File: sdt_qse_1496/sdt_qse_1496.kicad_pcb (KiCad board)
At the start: 2 copper layers, 100 x 70 mm, 88 parts, among them J1 Conn_02x08_Odd_Even, J2 SJ-3524-SMT, J3 5-1814832-1, J4 5-1814832-1, J6 Conn_01x02_Male, Q1 Q_NPN_BEC, Q2 Q_NPN_BEC, Q3 Q_PMOS_GSD, Q4 Q_PMOS_GSD, U1 SN74AC74PW, U2 MC1496DR2G, U3 Toroidal_Transformer, U4 MC1496DR2G

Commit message: Released to fab.
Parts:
- added C13: 0.1uF, Capacitor_SMD:C_1206_3216Metric, F.Cu at (120.5, 85.2)
- added C14: 0.1uF, Capacitor_SMD:C_1206_3216Metric, F.Cu at (116.1, 77.1)
- added R13: 100, Resistor_SMD:R_1206_3216Metric, F.Cu at (160.3, 117.3)
- added R15: 100, Resistor_SMD:R_1206_3216Metric, F.Cu at (146.1, 120.4)
- added R18: 100, Resistor_SMD:R_1206_3216Metric, F.Cu at (172.2, 122.8)
- moved R9 6.47 mm to (140.9, 87.8)
- moved R10 3.48 mm to (172.2, 126.3)
- moved C19 1.41 mm to (158.5, 111.8)
- moved C15 1.30 mm to (163.3, 113.4)
- moved R24 0.53 mm to (154.2, 108.9)
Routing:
- net Net-(R14-Pad1): track 23.9 -> 17.6 mm
- net GND: track 0.00 -> 4.88 mm, vias 65 -> 73
- net Net-(R10-Pad2): track 14.9 -> 19.1 mm
- net Net-(C4-Pad2): track 10.9 -> 14.4 mm
- net Net-(R8-Pad2): track 5.77 -> 9.08 mm
- net Net-(C8-Pad2): track 8.51 -> 11.1 mm
- net Net-(R12-Pad2): track 14.8 -> 17.1 mm
- net Net-(R62-Pad2): track 8.84 -> 10.7 mm
- net Net-(C15-Pad1): track 36.1 -> 34.5 mm
- net /12Vswitched: track 97.5 -> 96.6 mm
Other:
- board text added: "GREG KF5N"
- board text added: "PROTOTYPE 1"
- board text added: "QSE MC1496 EXCITER"

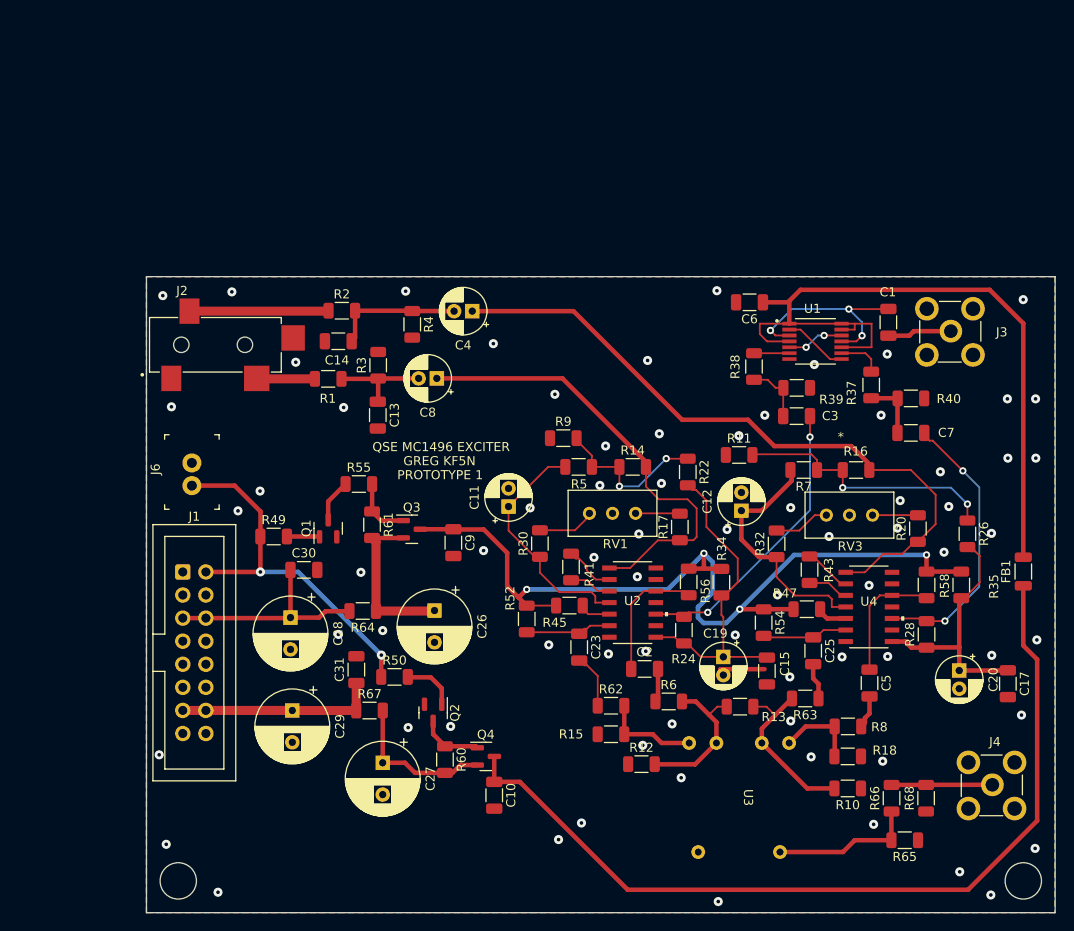
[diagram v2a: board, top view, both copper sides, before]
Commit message: Finishing layout of version2.
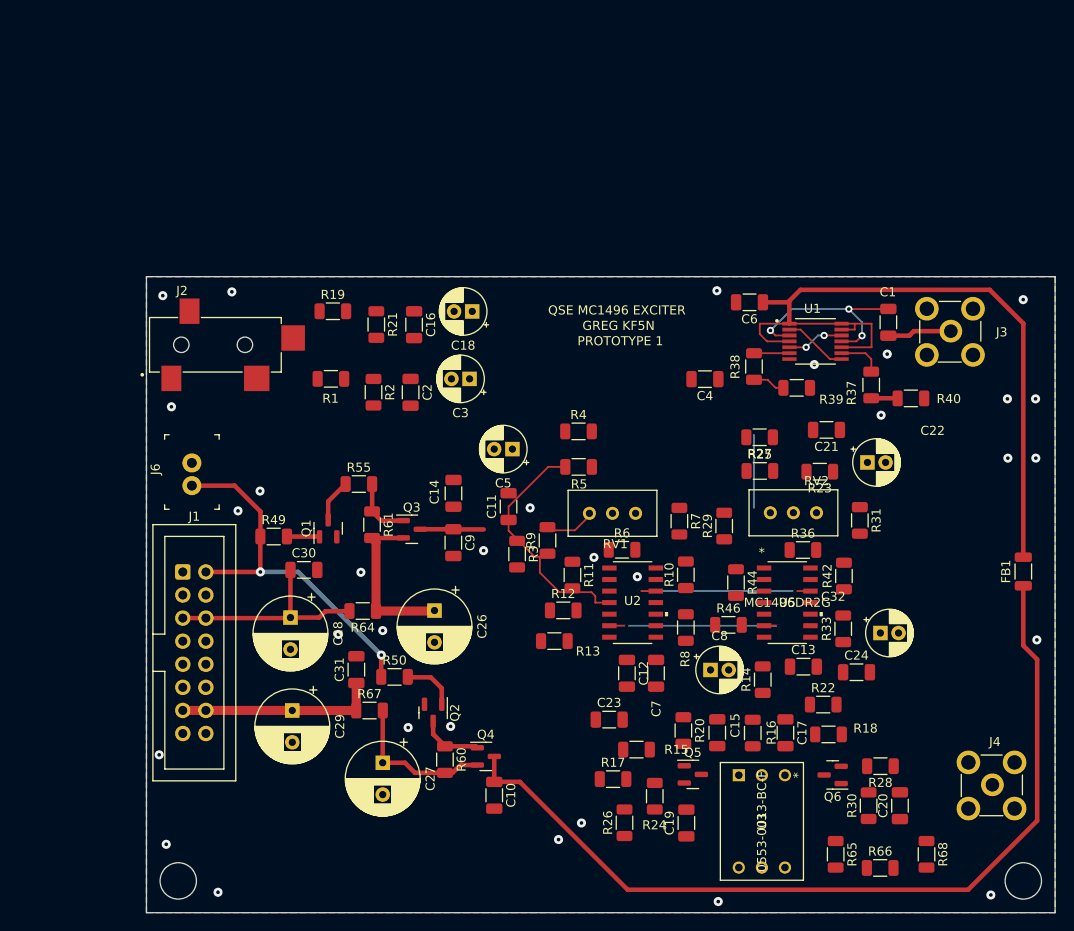
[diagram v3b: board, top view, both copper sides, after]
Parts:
- removed C25: 0.1uF, Capacitor_SMD:C_1206_3216Metric
- removed R32, R45, R47: 10k, Resistor_SMD:R_1206_3216Metric
- removed R34, R35: 1.3k, Resistor_SMD:R_1206_3216Metric
- removed R41, R43: 1.0k, Resistor_SMD:R_1206_3216Metric
- removed R52, R54, R56, R58: 3k, Resistor_SMD:R_1206_3216Metric
- removed R62, R63: 100, Resistor_SMD:R_1206_3216Metric
- removed RV3: 50k, Potentiometer_THT:Potentiometer_Bourns_3296W_Vertical
- removed U4: MC1496DR2G, MC1496:MC1496DR2G
- added C16: DNP, Capacitor_SMD:C_1206_3216Metric, F.Cu at (124.5, 75.3)
- added C18: 25uF 25V, Capacitor_THT:CP_Radial_D5.0mm_P2.00mm, F.Cu at (130.9, 73.8)
- added C21: 0.1uF, Capacitor_SMD:C_1206_3216Metric, F.Cu at (169.8, 86.9)
- added C22: 25uF 25V, Capacitor_THT:CP_Radial_D5.0mm_P2.00mm, F.Cu at (174.3, 90.5)
- added C24: 0.1uF, Capacitor_SMD:C_1206_3216Metric, F.Cu at (173.1, 113.5)
- added C32: 25uF 25V, Capacitor_THT:CP_Radial_D5.0mm_P2.00mm, F.Cu at (175.8, 109.2)
- added Q5: Q_NPN_BEC, Package_TO_SOT_SMD:SOT-23, F.Cu at (155.1, 124.8)
- added Q6: Q_NPN_BEC, Package_TO_SOT_SMD:SOT-23, F.Cu at (170.5, 124.8)
- added R19: 0, Resistor_SMD:R_1206_3216Metric, F.Cu at (115.5, 73.8)
- added R21: DNP, Resistor_SMD:R_1206_3216Metric, F.Cu at (120.3, 75.3)
- added R23: 1000, Resistor_SMD:R_1206_3216Metric, F.Cu at (169.1, 91.5)
- added R25: 1.0k, Resistor_SMD:R_1206_3216Metric, F.Cu at (162.5, 91.4)
- added R27: 1000, Resistor_SMD:R_1206_3216Metric, F.Cu at (162.5, 87.7)
- added R29: 10k, Resistor_SMD:R_1206_3216Metric, F.Cu at (158.6, 97.4)
- added R31: 820, Resistor_SMD:R_1206_3216Metric, F.Cu at (173.5, 96.8)
- added R33: 51, Resistor_SMD:R_1206_3216Metric, F.Cu at (171.7, 108.8)
- added R36: 10k, Resistor_SMD:R_1206_3216Metric, F.Cu at (167.3, 100.1)
- added R42: 1.3k, Resistor_SMD:R_1206_3216Metric, F.Cu at (171.8, 102.9)
- added R44: 500, Resistor_SMD:R_1206_3216Metric, F.Cu at (159.9, 103.7)
- added R46: 4700, Resistor_SMD:R_1206_3216Metric, F.Cu at (159.1, 108.3)
- added RV2: 50k, Potentiometer_THT:Potentiometer_Bourns_3296W_Vertical, F.Cu at (168.7, 96.0)
- added U5: MC1496DR2G, MC1496:MC1496DR2G, F.Cu at (165.5, 105.9)
- C11, C12, C19, C20, C4: value 25uF 25V -> 0.1uF; footprint Capacitor_THT:CP_Radial_D5.0mm_P2.00mm -> Capacitor_SMD:C_1206_3216Metric
- C2: value 0.1uF -> DNP
- C3, C5: value 0.1uF -> 25uF 25V; footprint Capacitor_SMD:C_1206_3216Metric -> Capacitor_THT:CP_Radial_D5.0mm_P2.00mm
- R1: value 100 -> 0
- R10: value 100 -> 1.3k
- R11: value 1.0k -> 500
- R12, R15, R16: value 100 -> 4700
- R13, R14: value 100 -> 500
- R17: value 10k -> 5100
- R18: value 100 -> 5100
- R2: value 100 -> DNP
- R20: value 10k -> 470
- R22: value 820 -> 470
- R24, R28: value 51 -> 10
- R26: value 820 -> 200
- R3, R5: value 100 -> 1000
- R30: value 10k -> 200
- R4: value 100 -> 1.0k
- R6: value 100 -> 10k
- R7: value 100 -> 820
- R8: value 100 -> 51
- R9: value 1.0k -> 10k
- U3: value Toroidal_Transformer -> 0553-0013-BC-F; footprint sdt_qse_1496:Toroidal_Transformer -> Pulse_Transformer:0553-0013-BC-F
- moved C13 54.4 mm to (167.3, 112.9), turned to 0 degrees
- moved R26 49.4 mm to (147.6, 130.1), turned to 90 degrees
- moved C5 47.0 mm to (135.3, 89.0), turned to 180 degrees
- moved R30 46.3 mm to (174.5, 128.2)
- moved C8 44.0 mm to (157.1, 113.3), turned to 0 degrees
- moved C2 39.9 mm to (124.1, 82.7), turned to -90 degrees
- moved C7 38.6 mm to (151.1, 113.7), turned to -90 degrees
- moved C3 36.2 mm to (130.6, 81.2), turned to 180 degrees
- moved R20 34.1 mm to (154.1, 120.0), turned to -90 degrees
- moved R16 31.1 mm to (161.7, 120.2), turned to -90 degrees
- moved R22 29.6 mm to (169.5, 117.1), turned to 0 degrees
- moved R10 29.5 mm to (154.4, 102.8), turned to 90 degrees
- moved R17 28.7 mm to (146.3, 125.3), turned to 0 degrees
- moved R14 27.4 mm to (162.8, 114.3), turned to 90 degrees
- moved C4 26.7 mm to (156.5, 81.3)
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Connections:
- net Net-(J2-Pad2) renamed /Double Balanced Modulator1/baseband_in
- C11 pad 1: Net-(C11-Pad1) -> /12Vswitched
- C12 pad 1: Net-(C12-Pad1) -> /Double Balanced Modulator/outplus
- C12 pad 2: GND -> Net-(C12-Pad2)
- C13 pad 1: Net-(C8-Pad2) -> /Double Balanced Modulator/outminus
- C13 pad 2: GND -> Net-(C13-Pad2)
- C14 pad 1: Net-(C4-Pad2) -> /12Vswitched
- C15 pad 2: GND -> Net-(C15-Pad2)
- C17 pad 2: GND -> Net-(C17-Pad2)
- C19 pad 1: Net-(C15-Pad1) -> GND
- C19 pad 2: GND -> Net-(C19-Pad2)
- C2 pad 2: Net-(C2-Pad2) -> GND
- C20 pad 1: Net-(C17-Pad1) -> GND
- C20 pad 2: GND -> Net-(C20-Pad2)
- C23 pad 1: Net-(C23-Pad1) -> GND
- C23 pad 2: Net-(C23-Pad2) -> /12Vswitched
- C3 pad 1: /LO_NINETY -> Net-(C3-Pad1)
- C3 pad 2: Net-(C3-Pad2) -> Net-(C2-Pad1)
- C4 pad 1: Net-(C4-Pad1) -> /LO_NINETY
- C5 pad 2: Net-(C5-Pad2) -> GND
- C7 pad 1: /LO_ZERO -> Net-(C7-Pad1)
- C7 pad 2: Net-(C7-Pad2) -> GND
- C8 pad 1: Net-(C8-Pad1) -> Net-(C7-Pad1)
- C8 pad 2: Net-(C8-Pad2) -> GND
- J2 pad 3: Net-(J2-Pad3) -> /Double Balanced Modulator/baseband_in
- R1 pad 2: Net-(C8-Pad2) -> Net-(C2-Pad1)
- R10 pad 1: GND -> Net-(C7-Pad1)
- R10 pad 2: Net-(R10-Pad2) -> /12Vswitched
- R11 pad 1: GND -> Net-(R11-Pad1)
- R12 pad 1: GND -> /12Vswitched
- R13 pad 1: Net-(R12-Pad2) -> /12Vswitched
- R13 pad 2: Net-(R10-Pad2) -> /Double Balanced Modulator/outplus
- R14 pad 1: Net-(R14-Pad1) -> /12Vswitched
- R14 pad 2: Net-(C8-Pad1) -> /Double Balanced Modulator/outminus
- R15 pad 1: GND -> Net-(C12-Pad2)
- R15 pad 2: Net-(R62-Pad2) -> /12Vswitched
- R16 pad 1: Net-(R11-Pad2) -> Net-(C13-Pad2)
- R16 pad 2: Net-(C4-Pad1) -> /12Vswitched
- R17 pad 1: Net-(C8-Pad1) -> GND
- R17 pad 2: Net-(R17-Pad2) -> Net-(C12-Pad2)
- R18 pad 1: Net-(R8-Pad2) -> GND
- R18 pad 2: GND -> Net-(C13-Pad2)
- R2 pad 1: Net-(J2-Pad3) -> Net-(C2-Pad1)
- R2 pad 2: Net-(C4-Pad2) -> GND
- R20 pad 1: Net-(C4-Pad1) -> Net-(C15-Pad1)
- R20 pad 2: Net-(R20-Pad2) -> Net-(C12-Pad2)
- R22 pad 1: Net-(R14-Pad1) -> Net-(C17-Pad1)
- R22 pad 2: Net-(C15-Pad1) -> Net-(C13-Pad2)
- R24 pad 1: Net-(C15-Pad1) -> Net-(C19-Pad2)
- R24 pad 2: Net-(C3-Pad2) -> Net-(Q5-Pad2)
- R26 pad 1: Net-(R11-Pad2) -> GND
- R26 pad 2: Net-(C17-Pad1) -> Net-(C19-Pad2)
- R28 pad 1: Net-(C17-Pad1) -> Net-(C20-Pad2)
- R28 pad 2: Net-(C7-Pad2) -> Net-(Q6-Pad2)
- R3 pad 1: Net-(C8-Pad2) -> Net-(R3-Pad1)
- R3 pad 2: GND -> Net-(C5-Pad1)
- R30 pad 1: Net-(C11-Pad1) -> GND
- R30 pad 2: Net-(R30-Pad2) -> Net-(C20-Pad2)
- R4 pad 1: Net-(C4-Pad2) -> GND
- R4 pad 2: GND -> Net-(R3-Pad1)
- R5 pad 1: Net-(R14-Pad1) -> Net-(R3-Pad1)
- R5 pad 2: Net-(C11-Pad1) -> Net-(C3-Pad1)
- R6 pad 1: Net-(C2-Pad2) -> Net-(C3-Pad1)
- R6 pad 2: Net-(R12-Pad2) -> Net-(R6-Pad2)
- R7 pad 1: Net-(R11-Pad2) -> Net-(R3-Pad1)
- R7 pad 2: Net-(C12-Pad1) -> Net-(C7-Pad1)
- R8 pad 1: Net-(C5-Pad2) -> Net-(C7-Pad1)
- R8 pad 2: Net-(R8-Pad2) -> Net-(C4-Pad2)
- R9 pad 1: GND -> Net-(C5-Pad1)
- R9 pad 2: Net-(R14-Pad1) -> Net-(R9-Pad2)
- RV1 pad 1: Net-(R30-Pad2) -> Net-(R9-Pad2)
- RV1 pad 3: Net-(R17-Pad2) -> Net-(R6-Pad2)
- U2 pad 1: Net-(C8-Pad1) -> Net-(C3-Pad1)
- U2 pad 10: Net-(C3-Pad2) -> Net-(C4-Pad2)
- U2 pad 12: Net-(C2-Pad1) -> /Double Balanced Modulator/outminus
- U2 pad 2: Net-(R41-Pad1) -> Net-(R11-Pad1)
- U2 pad 3: Net-(R41-Pad2) -> Net-(R11-Pad2)
- U2 pad 4: Net-(C11-Pad1) -> Net-(C5-Pad1)
- U2 pad 5: Net-(R45-Pad2) -> Net-(R12-Pad2)
- U2 pad 6: Net-(C23-Pad1) -> /Double Balanced Modulator/outplus
- U2 pad 8: Net-(C15-Pad1) -> Net-(C7-Pad1)
- U3 pad 1: Net-(R8-Pad2) -> Net-(C15-Pad2)
- U3 pad 2: Net-(R10-Pad2) -> GND
- U3 pad 3: Net-(R12-Pad2) -> /12Vswitched
- U3 pad 4: Net-(R62-Pad2) -> unconnected-(U3-Pad4)
- U3 pad 5: Net-(R65-Pad2) -> Net-(C17-Pad2)
- U3 pad 6: GND -> Net-(R65-Pad2)
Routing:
- net /12Vswitched: track 96.6 -> 7.00 mm, vias 4 -> 0
- net Net-(C4-Pad1): track 74.6 -> 0.00 mm
- net Net-(C8-Pad1): track 49.7 -> 0.00 mm
- net Net-(C15-Pad1): track 34.5 -> 0.00 mm
- net Net-(C3-Pad2): track 32.3 -> 0.00 mm, vias 2 -> 0
- net Net-(C7-Pad2): track 30.9 -> 0.00 mm, vias 2 -> 0
- net Net-(R11-Pad2): track 29.6 -> 0.00 mm, vias 2 -> 0
- net Net-(C17-Pad1): track 28.5 -> 0.00 mm
- net Net-(C12-Pad1): track 26.8 -> 0.00 mm
- net Net-(C11-Pad1): track 26.5 -> 0.00 mm
- net /Double Balanced Modulator/outminus: track 0.00 -> 20.7 mm, vias 0 -> 2
- net /Double Balanced Modulator/outplus: track 0.00 -> 20.2 mm, vias 0 -> 2
- net Net-(R10-Pad2): track 19.1 -> 0.00 mm
- net Net-(R14-Pad1): track 17.6 -> 0.00 mm, vias 2 -> 0
- net Net-(R12-Pad2): track 17.1 -> 0.00 mm
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
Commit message: Added gerbers for Prototype 2.
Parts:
- moved C14 31.3 mm to (143.7, 121.4), turned to 180 degrees
- moved C5 17.6 mm to (135.9, 106.5)
- moved C23 15.8 mm to (161.7, 120.2), turned to -90 degrees
- moved C21 15.0 mm to (181.1, 96.8), turned to -90 degrees
- moved R16 11.9 mm to (173.1, 116.6), turned to 0 degrees
- moved R36 10.4 mm to (177.1, 96.8), turned to -90 degrees
- moved R6 9.18 mm to (148.8, 91.0)
- moved R17 7.91 mm to (149.6, 118.1)
- moved C4 5.19 mm to (157.2, 86.4), turned to -90 degrees
- moved R4 3.97 mm to (142.6, 91.0)
- moved R5 3.17 mm to (142.6, 87.8)
- moved R22 2.41 mm to (167.3, 116.0)
- moved R13 1.00 mm to (140.9, 110.3)
- moved R11 0.96 mm to (142.5, 102.1)
- moved R15 0.95 mm to (149.6, 121.4)
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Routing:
- net /12Vswitched: track 7.00 -> 141.2 mm, vias 0 -> 4
- net Net-(C18-Pad1): track 0.00 -> 57.7 mm, vias 0 -> 2
- net Net-(C3-Pad1): track 0.00 -> 38.8 mm
- net Net-(C22-Pad1): track 0.00 -> 32.1 mm, vias 0 -> 1
- net Net-(C4-Pad2): track 0.00 -> 29.8 mm
- net Net-(R3-Pad1): track 0.00 -> 28.6 mm, vias 0 -> 2
- net Net-(C24-Pad1): track 0.00 -> 25.9 mm, vias 0 -> 1
- net Net-(C13-Pad2): track 0.00 -> 20.6 mm, vias 0 -> 2
- net Net-(R23-Pad1): track 0.00 -> 17.3 mm
- net Net-(J4-Pad2): track 0.00 -> 17.2 mm
- net Net-(C7-Pad1): track 8.05 -> 25.1 mm
- net Net-(C21-Pad2): track 0.00 -> 16.8 mm
- net /Double Balanced Modulator/baseband_in: track 0.00 -> 14.3 mm
- net /LO_ZERO: track 2.94 -> 16.3 mm
- net Net-(C12-Pad2): track 0.00 -> 13.2 mm
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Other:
- board text added: "PROTOTYPE 2"
- board text removed: "PROTOTYPE 1"

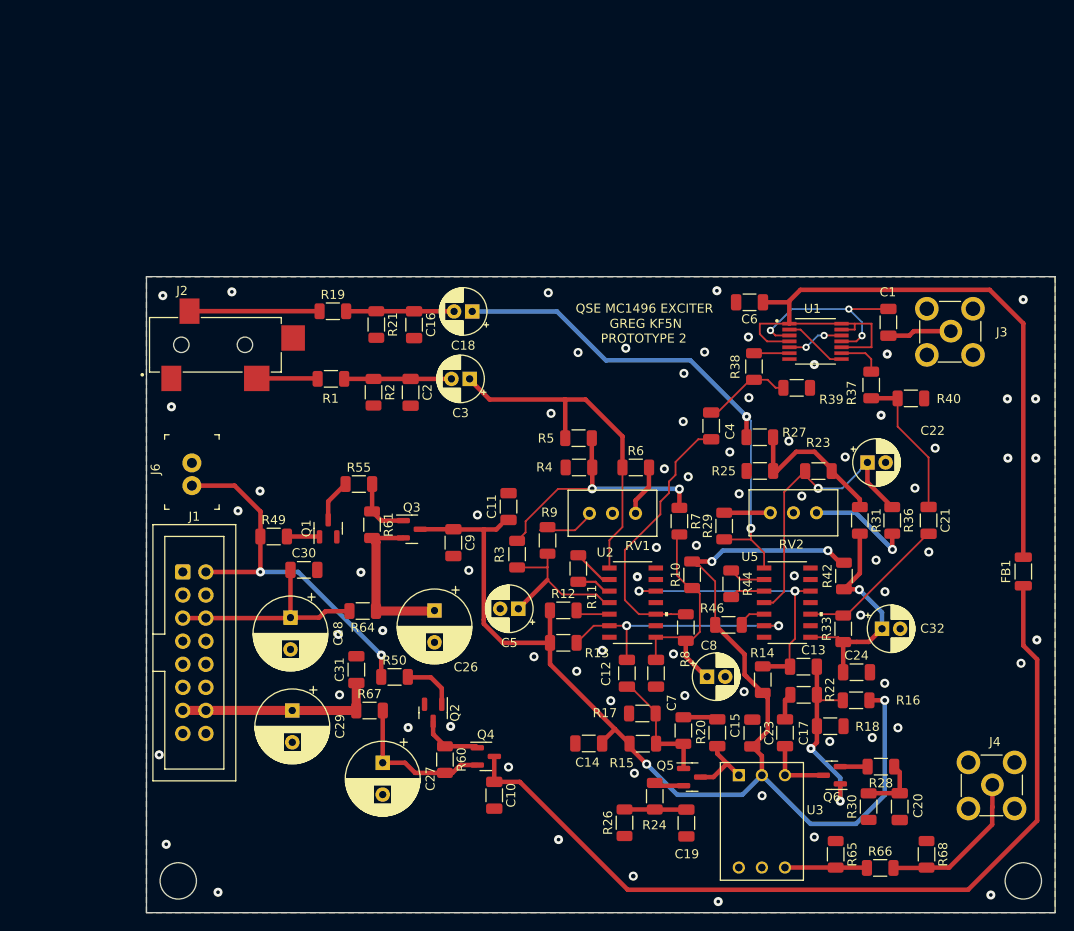
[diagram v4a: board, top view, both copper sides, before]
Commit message: Added Sallen Key filters to schematic.
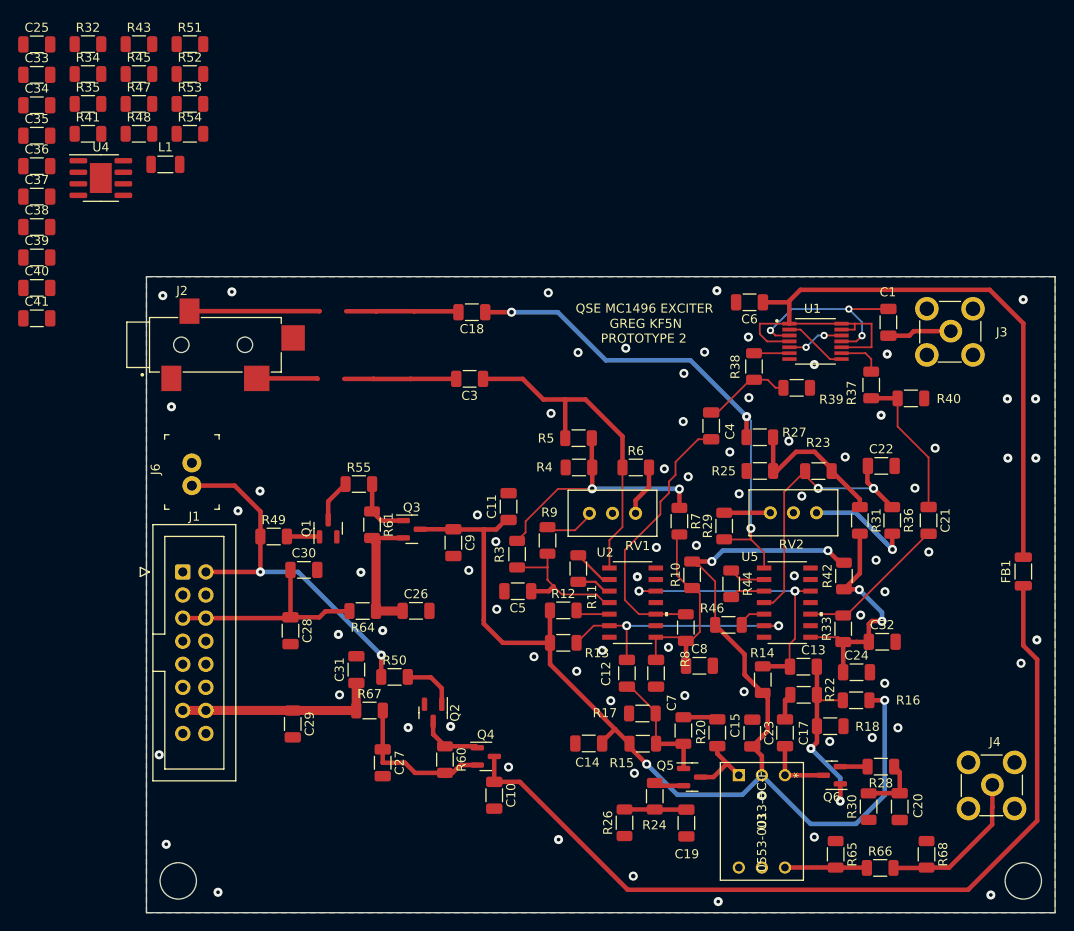
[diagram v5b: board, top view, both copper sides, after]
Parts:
- removed C16, C2: DNP, Capacitor_SMD:C_1206_3216Metric
- removed R1, R19: 0, Resistor_SMD:R_1206_3216Metric
- removed R2, R21: DNP, Resistor_SMD:R_1206_3216Metric
- added C25: 0.1uF, Capacitor_SMD:C_1206_3216Metric, F.Cu at (82.9, 44.4)
- added C33: 0.0033uF, Capacitor_SMD:C_1206_3216Metric, F.Cu at (82.9, 47.8)
- added C34: 0.0033uF, Capacitor_SMD:C_1206_3216Metric, F.Cu at (82.9, 51.1)
- added C35: 0.0033uF, Capacitor_SMD:C_1206_3216Metric, F.Cu at (82.9, 54.5)
- added C36: 0.0033uF, Capacitor_SMD:C_1206_3216Metric, F.Cu at (82.9, 57.8)
- added C37: 22uF 16V, Capacitor_SMD:C_1206_3216Metric, F.Cu at (82.9, 61.2)
- added C38: 22uF 16V, Capacitor_SMD:C_1206_3216Metric, F.Cu at (82.9, 64.5)
- added C39: 22uF 16V, Capacitor_SMD:C_1206_3216Metric, F.Cu at (82.9, 67.9)
- added C40: 22uF 16V, Capacitor_SMD:C_1206_3216Metric, F.Cu at (82.9, 71.2)
- added C41: 22uF 16V, Capacitor_SMD:C_1206_3216Metric, F.Cu at (82.9, 74.6)
- added L1: Ferrite 600, Inductor_SMD:L_1206_3216Metric, F.Cu at (97.1, 57.6)
- added R32: 100K, Resistor_SMD:R_1206_3216Metric, F.Cu at (88.6, 44.4)
- added R34: 100K, Resistor_SMD:R_1206_3216Metric, F.Cu at (88.6, 47.7)
- added R35: 100K, Resistor_SMD:R_1206_3216Metric, F.Cu at (88.6, 51.0)
- added R41: 100K, Resistor_SMD:R_1206_3216Metric, F.Cu at (88.6, 54.3)
- added R43: 3.6K, Resistor_SMD:R_1206_3216Metric, F.Cu at (94.2, 44.4)
- added R45: 3.6K, Resistor_SMD:R_1206_3216Metric, F.Cu at (94.2, 47.7)
- added R47: 5.1K, Resistor_SMD:R_1206_3216Metric, F.Cu at (94.2, 51.0)
- added R48: 5.1K, Resistor_SMD:R_1206_3216Metric, F.Cu at (94.2, 54.3)
- added R51: 5.1K, Resistor_SMD:R_1206_3216Metric, F.Cu at (99.8, 44.4)
- added R52: 5.1K, Resistor_SMD:R_1206_3216Metric, F.Cu at (99.8, 47.7)
- added R53: 5.1K, Resistor_SMD:R_1206_3216Metric, F.Cu at (99.8, 51.0)
- added R54: 5.1K, Resistor_SMD:R_1206_3216Metric, F.Cu at (99.8, 54.3)
- added U4: LM4562, Package_SO:SOIC-8-1EP_3.9x4.9mm_P1.27mm_EP2.41x3.3mm, F.Cu at (90.0, 59.1)
- C18, C3, C32, C8: value 25uF 25V -> 22uF 16V; footprint Capacitor_THT:CP_Radial_D5.0mm_P2.00mm -> Capacitor_SMD:C_1206_3216Metric
- C22, C5: footprint Capacitor_THT:CP_Radial_D5.0mm_P2.00mm -> Capacitor_SMD:C_1206_3216Metric
- C26, C27, C28, C29: value 100uF 25V -> 22uF 16V; footprint Capacitor_THT:CP_Radial_D8.0mm_P3.50mm -> Capacitor_SMD:C_1206_3216Metric
- R13, R14: value 500 -> 470
- R37, R38: value 10k -> 470
- R39, R40: value 10k -> 100
- R65, R68: value 100 -> DNP
- R66: value 100 -> 0
- U3: footprint Pulse_Transformer:0553-0013-BC-F -> 0553-0013_BEL:0553-0013-BC-F
- moved C26 2.04 mm to (124.7, 106.8), turned to 0 degrees
- moved C5 1.93 mm to (135.9, 104.6)
- moved C22 1.57 mm to (175.9, 90.8)
- moved C29 1.48 mm to (111.1, 119.2)
- moved C8 1.46 mm to (155.9, 112.8)
- moved C28 1.44 mm to (110.8, 109.0)
- moved C32 1.44 mm to (176.0, 110.2)
- moved C18 0.10 mm to (130.8, 73.9)
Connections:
- C17 pad 2: Net-(C17-Pad2) -> Net-(Q6-C)
- C18 pad 2: Net-(C16-Pad1) -> /Double Balanced Modulator/baseband_in
- C3 pad 2: Net-(C2-Pad1) -> /Double Balanced Modulator1/baseband_in
- J2 pad 2: /Double Balanced Modulator1/baseband_in -> /SallenKeyFilters/TX_RAW_I_IN
- J2 pad 3: /Double Balanced Modulator/baseband_in -> /SallenKeyFilters/TX_RAW_Q_IN
- Q6 pad 3: Net-(C17-Pad2) -> Net-(Q6-C)
- U3 pad 2: GND -> /12Vswitched
- U3 pad 3: /12Vswitched -> Net-(Q6-C)
- U3 pad 4: unconnected-(U3-Pad4) -> Net-(R65-Pad2)
- U3 pad 5: Net-(C17-Pad2) -> unconnected-(U3-Pad5)
- U3 pad 6: Net-(R65-Pad2) -> GND
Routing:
- net /SallenKeyFilters/TX_RAW_Q_IN: track 0.00 -> 14.3 mm
- net Net-(C16-Pad1): track 11.9 -> 0.00 mm
- net Net-(C2-Pad1): track 11.8 -> 0.00 mm
- net Net-(Q6-C): track 0.00 -> 7.42 mm
- net Net-(C17-Pad2): track 7.42 -> 0.00 mm
- net /SallenKeyFilters/TX_RAW_I_IN: track 0.00 -> 6.72 mm
- net /Double Balanced Modulator1/baseband_in: track 6.72 -> 11.8 mm
- net Net-(Q3-S): track 18.1 -> 14.6 mm
- net Net-(U2-INPUTCARRIER): track 25.1 -> 21.7 mm
- net /Double Balanced Modulator/baseband_in: track 14.3 -> 11.9 mm
- net Net-(C5-Pad1): track 18.6 -> 16.8 mm
- net Net-(C3-Pad1): track 38.8 -> 37.3 mm
- net Net-(C18-Pad1): track 57.7 -> 56.2 mm, vias 2 -> 3
- net Net-(U5-INPUTCARRIER): track 25.9 -> 26.6 mm, vias 1 -> 2
- net Net-(C22-Pad1): track 32.1 -> 31.6 mm, vias 1 -> 2
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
